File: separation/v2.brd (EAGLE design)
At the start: 8 parts

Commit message: routed
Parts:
- moved SERCON 2.84 mm to (14.0, 14.0)
- moved BAT 2.84 mm to (14.1, 19.4)
- moved MCU-L 2.84 mm to (6.35, 21.4)
- moved MCU-R 2.84 mm to (-8.89, 21.4)
- moved R1 2.84 mm to (14.1, 28.3)
- moved LDO 2.84 mm to (-15.2, 17.0)
- moved LOUD 2.84 mm to (-17.8, 26.7)
- moved R2 2.84 mm to (11.3, 28.3)
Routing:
- net BUZZ: track 0.00 -> 43.5 mm
- net VSENSE: track 0.00 -> 17.5 mm
- net VCC: track 0.00 -> 13.8 mm
- net SERVO: track 0.00 -> 7.17 mm

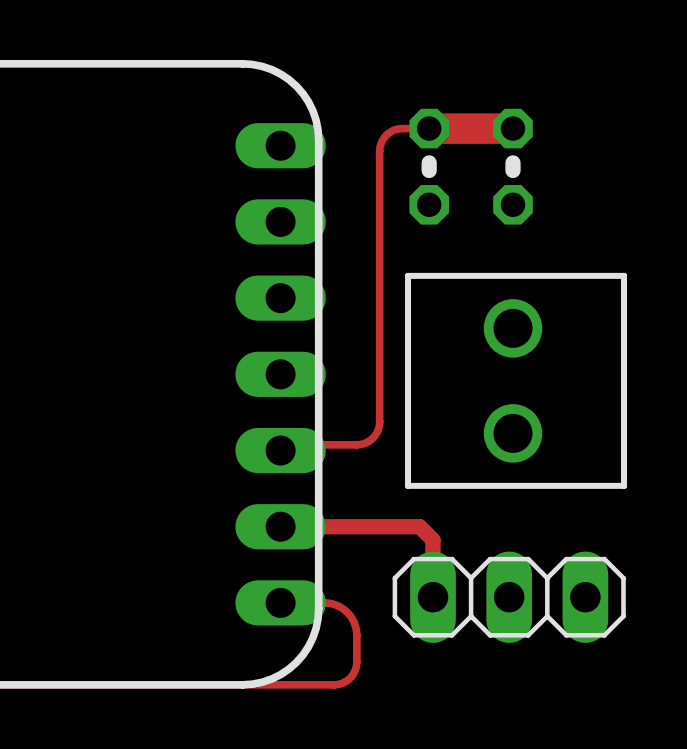
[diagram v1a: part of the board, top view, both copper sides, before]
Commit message: shuffle right group down
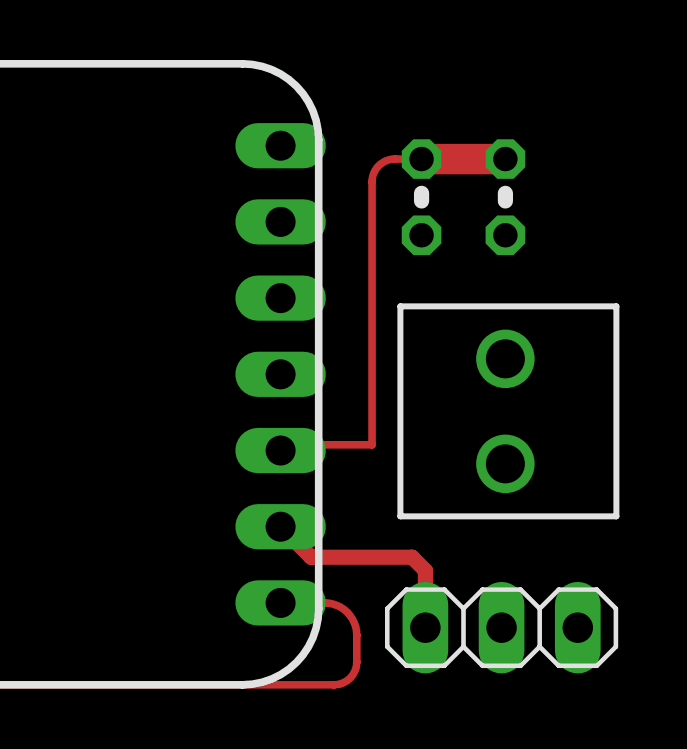
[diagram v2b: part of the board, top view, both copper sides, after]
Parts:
- moved R2 1.05 mm to (11.0, 27.3)
- moved BAT 1.05 mm to (13.8, 18.4)
- moved R1 1.05 mm to (13.8, 27.3)
- moved SERCON 1.05 mm to (13.7, 13.0)
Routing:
- net VSENSE: track 17.5 -> 16.7 mm
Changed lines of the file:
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@@
 <attribute name="RS_PRICE-STOCK" value="http://uk.rs-online.com/web/p/products/2988508P" x="-15.24" y="17.018" size="1.778" layer="27" font="vector" ratio="15" rot="R180" display="off"/>
 </element>
-<element name="BAT" library="SamacSys_Parts" package="MB332350M02SZ" value="MB332-350M02SZ" x="14.097" y="19.431" smashed="yes" rot="R90">
-<attribute name="DESCRIPTION" value="RS PRO 3.5mm Pitch Straight, PCB Terminal Block, Through Hole, 2 Way" x="14.097" y="19.431" size="1.778" layer="27" font="vector" ratio="15" rot="R90" display="off"/>
-<attribute name="HEIGHT" value="12.76mm" x="14.097" y="19.431" size="1.778" layer="27" font="vector" ratio="15" rot="R90" display="off"/>
-<attribute name="MANUFACTURER_NAME" value="RS Components" x="14.097" y="19.431" size="1.778" layer="27" font="vector" ratio="15" rot="R90" display="off"/>
-<attribute name="MANUFACTURER_PART_NUMBER" value="MB332-350M02SZ" x="14.097" y="19.431" size="1.778" layer="27" font="vector" ratio="15" rot="R90" display="off"/>
-<attribute name="RS_PART_NUMBER" value="7901149" x="14.097" y="19.431" size="1.778" layer="27" font="vector" ratio="15" rot="R90" display="off"/>
-<attribute name="RS_PRICE-STOCK" value="https://uk.rs-online.com/web/p/products/7901149" x="14.097" y="19.431" size="1.778" layer="27" font="vector" ratio="15" rot="R90" display="off"/>
+<element name="BAT" library="SamacSys_Parts" package="MB332350M02SZ" value="MB332-350M02SZ" x="13.843" y="18.415" smashed="yes" rot="R90">
+<attribute name="DESCRIPTION" value="RS PRO 3.5mm Pitch Straight, PCB Terminal Block, Through Hole, 2 Way" x="13.843" y="18.415" size="1.778" layer="27" font="vector" ratio="15" rot="R90" display="off"/>
+<attribute name="HEIGHT" value="12.76mm" x="13.843" y="18.415" size="1.778" layer="27" font="vector" ratio="15" rot="R90" display="off"/>
+<attribute name="MANUFACTURER_NAME" value="RS Components" x="13.843" y="18.415" size="1.778" layer="27" font="vector" ratio="15" rot="R90" display="off"/>
+<attribute name="MANUFACTURER_PART_NUMBER" value="MB332-350M02SZ" x="13.843" y="18.415" size="1.778" layer="27" font="vector" ratio="15" rot="R90" display="off"/>
+<attribute name="RS_PART_NUMBER" value="7901149" x="13.843" y="18.415" size="1.778" layer="27" font="vector" ratio="15" rot="R90" display="off"/>
+<attribute name="RS_PRICE-STOCK" value="https://uk.rs-online.com/web/p/products/7901149" x="13.843" y="18.415" size="1.778" layer="27" font="vector" ratio="15" rot="R90" display="off"/>
 </element>
-<element name="SERCON" library="pinhead" library_urn="urn:adsk.eagle:library:325" package="1X03" package3d_urn="urn:adsk.eagle:package:22458/2" value="" x="13.97" y="13.97" smashed="yes" rot="R180">
-<attribute name="POPULARITY" value="92" x="13.97" y="13.97" size="1.778" layer="27" font="vector" ratio="15" rot="R180" display="off"/>
-<attribute name="VALUE" x="17.78" y="17.145" size="1.27" layer="27" rot="R180"/>
+<element name="SERCON" library="pinhead" library_urn="urn:adsk.eagle:library:325" package="1X03" package3d_urn="urn:adsk.eagle:package:22458/2" value="" x="13.716" y="12.954" smashed="yes" rot="R180">
+<attribute name="POPULARITY" value="92" x="13.716" y="12.954" size="1.778" layer="27" font="vector" ratio="15" rot="R180" display="off"/>
+<attribute name="VALUE" x="17.526" y="16.129" size="1.27" layer="27" rot="R180"/>
 </element>
-<element name="R1" library="rcl" library_urn="urn:adsk.eagle:library:334" package="0204V" package3d_urn="urn:adsk.eagle:package:23495/1" value="220k" x="14.097" y="28.321" smashed="yes" rot="R90">
-<attribute name="POPULARITY" value="11" x="14.097" y="28.321" size="1.778" layer="27" font="vector" ratio="15" rot="R90" display="off"/>
-<attribute name="SPICEPREFIX" value="R" x="14.097" y="28.321" size="1.778" layer="27" font="vector" ratio="15" rot="R90" display="off"/>
-<attribute name="VALUE" x="19.0246" y="27.2796" size="0.9906" layer="27" ratio="10" rot="R180"/>
+<element name="R1" library="rcl" library_urn="urn:adsk.eagle:library:334" package="0204V" package3d_urn="urn:adsk.eagle:package:23495/1" value="220k" x="13.843" y="27.305" smashed="yes" rot="R90">
+<attribute name="POPULARITY" value="11" x="13.843" y="27.305" size="1.778" layer="27" font="vector" ratio="15" rot="R90" display="off"/>
+<attribute name="SPICEPREFIX" value="R" x="13.843" y="27.305" size="1.778" layer="27" font="vector" ratio="15" rot="R90" display="off"/>
+<attribute name="VALUE" x="18.7706" y="26.2636" size="0.9906" layer="27" ratio="10" rot="R180"/>
 </element>
-<element name="R2" library="rcl" library_urn="urn:adsk.eagle:library:334" package="0204V" package3d_urn="urn:adsk.eagle:package:23495/1" value="120k" x="11.303" y="28.321" smashed="yes" rot="R270">
-<attribute name="POPULARITY" value="11" x="11.303" y="28.321" size="1.778" layer="27" font="vector" ratio="15" rot="R270" display="off"/>
-<attribute name="SPICEPREFIX" value="R" x="11.303" y="28.321" size="1.778" layer="27" font="vector" ratio="15" rot="R270" display="off"/>
-<attribute name="VALUE" x="8.1534" y="31.1404" size="0.9906" layer="27" ratio="10"/>
+<element name="R2" library="rcl" library_urn="urn:adsk.eagle:library:334" package="0204V" package3d_urn="urn:adsk.eagle:package:23495/1" value="120k" x="11.049" y="27.305" smashed="yes" rot="R270">
+<attribute name="POPULARITY" value="11" x="11.049" y="27.305" size="1.778" layer="27" font="vector" ratio="15" rot="R270" display="off"/>
+<attribute name="SPICEPREFIX" value="R" x="11.049" y="27.305" size="1.778" layer="27" font="vector" ratio="15" rot="R270" display="off"/>
+<attribute name="VALUE" x="7.8994" y="30.1244" size="0.9906" layer="27" ratio="10"/>
 </element>
 </elements>
@@
 <contactref element="LOUD" pad="2"/>
 <contactref element="R2" pad="2"/>
-<wire x1="13.97" y1="13.97" x2="14.097" y2="22.931" width="0" layer="19" extent="1-1"/>
-<wire x1="-17.79" y1="17.018" x2="13.97" y2="13.97" width="0" layer="19" extent="1-1"/>
+<wire x1="13.716" y1="12.954" x2="13.843" y2="21.915" width="0" layer="19" extent="1-1"/>
+<wire x1="-17.79" y1="17.018" x2="13.716" y2="12.954" width="0" layer="19" extent="1-1"/>
 <wire x1="-17.78" y1="22.67" x2="-17.79" y2="17.018" width="0" layer="19" extent="1-1"/>
-<wire x1="11.303" y1="27.051" x2="-17.78" y2="22.67" width="0" layer="19" extent="1-1"/>
-<wire x1="-8.89" y1="16.3195" x2="11.303" y2="27.051" width="0" layer="19" extent="1-1"/>
+<wire x1="11.049" y1="26.035" x2="-17.78" y2="22.67" width="0" layer="19" extent="1-1"/>
+<wire x1="-8.89" y1="16.3195" x2="11.049" y2="26.035" width="0" layer="19" extent="1-1"/>
 </signal>
 <signal name="MOSI">
@@
 <contactref element="LDO" pad="1"/>
 <contactref element="R1" pad="1"/>
-<wire x1="16.51" y1="13.97" x2="14.097" y2="19.431" width="0" layer="19" extent="1-1"/>
-<wire x1="-15.24" y1="17.018" x2="16.51" y2="13.97" width="0" layer="19" extent="1-1"/>
-<wire x1="14.097" y1="27.051" x2="-15.24" y2="17.018" width="0" layer="19" extent="1-1"/>
+<wire x1="16.256" y1="12.954" x2="13.843" y2="18.415" width="0" layer="19" extent="1-1"/>
+<wire x1="-15.24" y1="17.018" x2="16.256" y2="12.954" width="0" layer="19" extent="1-1"/>
+<wire x1="13.843" y1="26.035" x2="-15.24" y2="17.018" width="0" layer="19" extent="1-1"/>
 </signal>
 <signal name="SERVO">
 <contactref element="SERCON" pad="3"/>
 <contactref element="MCU-L" pad="2"/>
-<wire x1="6.35" y1="16.3195" x2="10.9855" y2="16.3195" width="0.508" layer="1"/>
-<wire x1="10.9855" y1="16.3195" x2="11.43" y2="15.875" width="0.508" layer="1"/>
-<wire x1="11.43" y1="15.875" x2="11.43" y2="13.97" width="0.508" layer="1"/>
+<wire x1="10.7315" y1="15.3035" x2="7.366" y2="15.3035" width="0.508" layer="1"/>
+<wire x1="6.35" y1="16.3195" x2="7.366" y2="15.3035" width="0.508" layer="1"/>
+<wire x1="10.7315" y1="15.3035" x2="11.176" y2="14.859" width="0.508" layer="1"/>
+<wire x1="11.176" y1="14.859" x2="11.176" y2="12.954" width="0.508" layer="1"/>
 </signal>
 <signal name="BUZZ">
@@
 <contactref element="R2" pad="1"/>
 <contactref element="MCU-L" pad="3"/>
-<wire x1="11.303" y1="29.591" x2="14.097" y2="29.591" width="1.016" layer="1"/>
-<wire x1="11.303" y1="29.591" x2="10.414" y2="29.591" width="0.254" layer="1"/>
-<wire x1="10.414" y1="29.591" x2="9.652" y2="28.829" width="0.254" layer="1" curve="90"/>
-<wire x1="9.652" y1="19.812" x2="8.89" y2="19.05" width="0.254" layer="1" curve="-90"/>
-<wire x1="8.89" y1="19.05" x2="6.5405" y2="19.05" width="0.254" layer="1"/>
+<wire x1="11.049" y1="28.575" x2="13.843" y2="28.575" width="1.016" layer="1"/>
+<wire x1="11.049" y1="28.575" x2="10.16" y2="28.575" width="0.254" layer="1"/>
+<wire x1="10.16" y1="28.575" x2="9.398" y2="27.813" width="0.254" layer="1" curve="90"/>
+<wire x1="9.398" y1="19.05" x2="6.5405" y2="19.05" width="0.254" layer="1"/>
 <wire x1="6.5405" y1="19.05" x2="6.35" y2="18.8595" width="0.254" layer="1" curve="90"/>
-<wire x1="9.652" y1="28.829" x2="9.652" y2="19.812" width="0.254" layer="1"/>
+<wire x1="9.398" y1="27.813" x2="9.398" y2="19.05" width="0.254" layer="1"/>
 </signal>
 </signals>

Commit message: draw intiial outline
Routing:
- net BUZZ: track 43.5 -> 40.4 mm
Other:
- board outline added: 43.2 x 22.9 mm
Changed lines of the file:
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@@
 <wire x1="-8.89" y1="26.543" x2="-10.668" y2="26.543" width="1.524" layer="29"/>
 <wire x1="-8.89" y1="29.083" x2="-10.668" y2="29.083" width="1.524" layer="29"/>
+<wire x1="-12.7" y1="33.02" x2="-24.13" y2="21.59" width="0.254" layer="20" curve="90"/>
+<wire x1="-24.13" y1="21.59" x2="-24.13" y2="12.7" width="0.254" layer="20"/>
+<wire x1="-24.13" y1="12.7" x2="-21.59" y2="10.16" width="0.254" layer="20" curve="90"/>
+<wire x1="-21.59" y1="10.16" x2="16.51" y2="10.16" width="0.254" layer="20"/>
+<wire x1="16.51" y1="10.16" x2="19.05" y2="12.7" width="0.254" layer="20" curve="90"/>
+<wire x1="19.05" y1="12.7" x2="19.05" y2="24.13" width="0.254" layer="20"/>
+<wire x1="10.16" y1="33.02" x2="19.05" y2="24.13" width="0.254" layer="20" curve="-90"/>
+<wire x1="10.16" y1="33.02" x2="-12.7" y2="33.02" width="0.254" layer="20"/>
 </plain>
 <attributes>
@@
 <contactref element="LOUD" pad="1"/>
 <contactref element="MCU-L" pad="1"/>
-<wire x1="6.35" y1="13.7795" x2="7.8105" y2="13.7795" width="0.254" layer="1"/>
-<wire x1="7.8105" y1="13.7795" x2="8.89" y2="12.7" width="0.254" layer="1" curve="-90"/>
-<wire x1="8.89" y1="12.7" x2="8.89" y2="11.811" width="0.254" layer="1"/>
-<wire x1="8.89" y1="11.811" x2="8.128" y2="11.049" width="0.254" layer="1" curve="-90"/>
-<wire x1="-10.795" y1="11.049" x2="-13.335" y2="13.589" width="0.254" layer="1" curve="-90"/>
+<wire x1="-13.335" y1="13.589" x2="-10.795" y2="11.049" width="0.254" layer="1" curve="90"/>
 <wire x1="-13.335" y1="24.13" x2="-15.875" y2="26.67" width="0.254" layer="1" curve="90"/>
 <wire x1="-15.875" y1="26.67" x2="-17.78" y2="26.67" width="0.254" layer="1"/>
-<wire x1="8.128" y1="11.049" x2="-10.795" y2="11.049" width="0.254" layer="1"/>
 <wire x1="-13.335" y1="13.589" x2="-13.335" y2="24.13" width="0.254" layer="1"/>
+<wire x1="-10.795" y1="11.049" x2="-2.54" y2="11.049" width="0.254" layer="1"/>
+<wire x1="-2.54" y1="11.049" x2="5.969" y2="11.049" width="0.254" layer="1"/>
+<wire x1="5.969" y1="11.049" x2="7.62" y2="12.7" width="0.254" layer="1" curve="90"/>
+<wire x1="7.62" y1="12.7" x2="6.5405" y2="13.7795" width="0.254" layer="1" curve="90"/>
+<wire x1="6.5405" y1="13.7795" x2="6.35" y2="13.7795" width="0.254" layer="1"/>
 </signal>
 <signal name="VSENSE">

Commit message: move buzzer PWM out to MISO pin
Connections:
- removed net MISO: MCU-R.3
- new net A0: MCU-L.1
- net BUZZ: now also MCU-R.3; no longer MCU-L.1
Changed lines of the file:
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@@
 <contactref element="MCU-R" pad="4"/>
-</signal>
-<signal name="MISO">
-<contactref element="MCU-R" pad="3"/>
 </signal>
 <signal name="SCK">
@@
 <signal name="BUZZ">
 <contactref element="LOUD" pad="1"/>
-<contactref element="MCU-L" pad="1"/>
 <wire x1="-13.335" y1="13.589" x2="-10.795" y2="11.049" width="0.254" layer="1" curve="90"/>
 <wire x1="-13.335" y1="24.13" x2="-15.875" y2="26.67" width="0.254" layer="1" curve="90"/>
@@
 <wire x1="5.969" y1="11.049" x2="7.62" y2="12.7" width="0.254" layer="1" curve="90"/>
 <wire x1="7.62" y1="12.7" x2="6.5405" y2="13.7795" width="0.254" layer="1" curve="90"/>
-<wire x1="6.5405" y1="13.7795" x2="6.35" y2="13.7795" width="0.254" layer="1"/>
+<contactref element="MCU-R" pad="3"/>
+<wire x1="-17.78" y1="26.67" x2="-8.89" y2="23.9395" width="0" layer="19" extent="1-1"/>
 </signal>
 <signal name="VSENSE">
@@
 <wire x1="9.398" y1="27.813" x2="9.398" y2="19.05" width="0.254" layer="1"/>
 </signal>
+<signal name="A0">
+<contactref element="MCU-L" pad="1"/>
+</signal>
 </signals>
